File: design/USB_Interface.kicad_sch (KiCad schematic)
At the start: 7 parts, among them J6 USB_C_Receptacle_USB2.0_16P

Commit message: Correccion de algunos DRC
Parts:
- R38: LCSC (none) -> C95177
- R39: LCSC (none) -> C114668
- R40, R41: LCSC (none) -> C107701
- R42, R43: LCSC (none) -> C105580
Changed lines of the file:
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@@
+			)
+		)
+		(property "LCSC" "C107701"
+			(at 138.43 99.06 0)
+			(effects
+				(font
+					(size 1.27 1.27)
+				)
+				(hide yes)
 			)
 		)
@@
 		)
 		(property "MPN" "RC0603FR-075K1L"
+			(at 167.64 107.95 0)
+			(effects
+				(font
+					(size 1.27 1.27)
+				)
+				(hide yes)
+			)
+		)
+		(property "LCSC" "C105580"
 			(at 167.64 107.95 0)
 			(effects
@@
 			)
 		)
+		(property "LCSC" "C95177"
+			(at 111.76 81.28 0)
+			(effects
+				(font
+					(size 1.27 1.27)
+				)
+				(hide yes)
+			)
+		)
 		(pin "1"
 		)
@@
 			)
 		)
+		(property "LCSC" "C107701"
+			(at 138.43 93.98 0)
+			(effects
+				(font
+					(size 1.27 1.27)
+				)
+				(hide yes)
+			)
+		)
 		(pin "1"
 		)
@@
 			)
 		)
+		(property "LCSC" "C105580"
+			(at 157.48 107.95 0)
+			(effects
+				(font
+					(size 1.27 1.27)
+				)
+				(hide yes)
+			)
+		)
 		(pin "1"
 		)
@@
 			(at 121.92 101.6 0)
 			(effects
+				(font
+					(size 1.27 1.27)
+				)
+				(hide yes)
+			)
+		)
+		(property "LCSC" "C114668"
+			(at 121.92 101.6 0)
+			(effects

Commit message: Abaratando costos
Cambios en numeros de jlcpcb, pasados a componentes básicos
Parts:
- J6: now left out of the parts list
- R38: LCSC C95177 -> C21189
- R39: LCSC C114668 -> C22843
- R40, R41: LCSC C107701 -> C23345
- R42, R43: LCSC C105580 -> C23186
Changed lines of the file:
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@@
 			)
 		)
-		(property "LCSC" "C107701"
+		(property "LCSC" "C23345"
 			(at 138.43 99.06 0)
 			(effects
@@
 			)
 		)
-		(property "LCSC" "C105580"
+		(property "LCSC" "C23186"
 			(at 167.64 107.95 0)
 			(effects
@@
 		(unit 1)
 		(exclude_from_sim no)
-		(in_bom yes)
+		(in_bom no)
 		(on_board yes)
 		(dnp no)
@@
 			)
 		)
-		(property "LCSC" "C95177"
+		(property "LCSC" "C21189"
 			(at 111.76 81.28 0)
 			(effects
@@
 			)
 		)
-		(property "LCSC" "C107701"
+		(property "LCSC" "C23345"
 			(at 138.43 93.98 0)
 			(effects
@@
 			)
 		)
-		(property "LCSC" "C105580"
+		(property "LCSC" "C23186"
 			(at 157.48 107.95 0)
 			(effects
@@
 			)
 		)
-		(property "LCSC" "C114668"
+		(property "LCSC" "C22843"
 			(at 121.92 101.6 0)
 			(effects

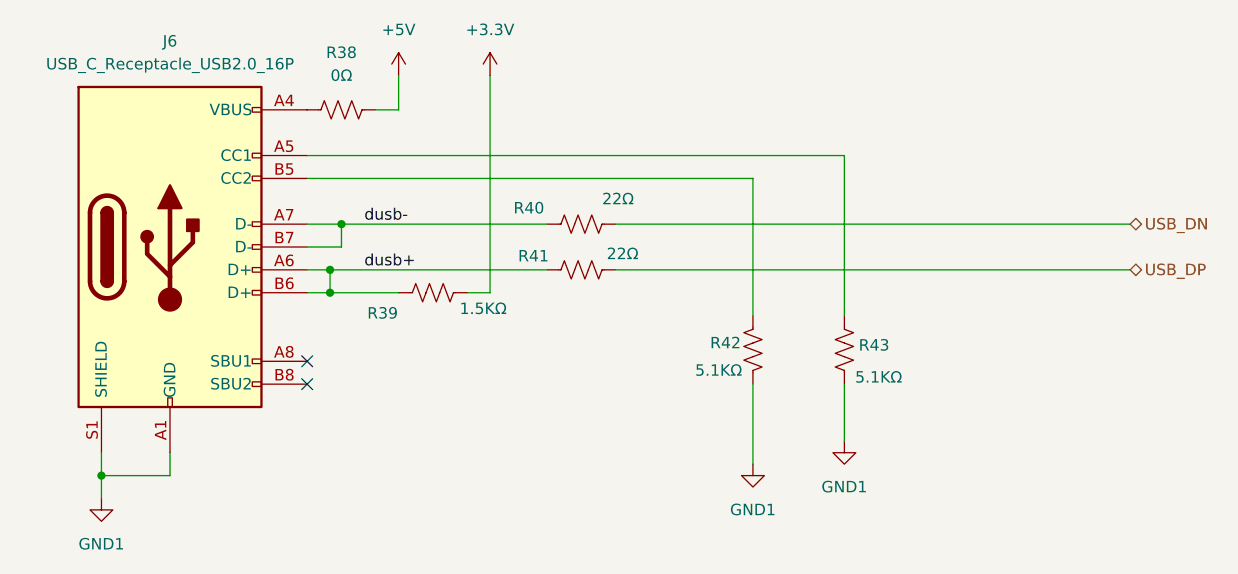
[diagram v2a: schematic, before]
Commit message: Sacado de NRF
Sacado de NRF, re-hecho constraints
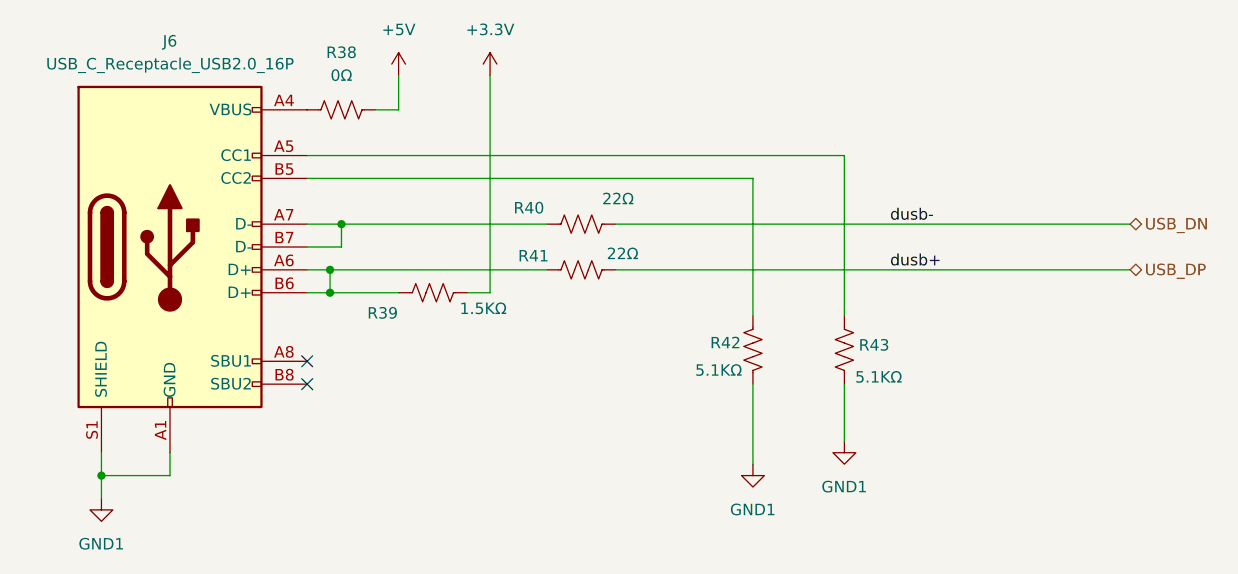
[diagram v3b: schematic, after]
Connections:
- net dusb+: no longer names the net of J6.A6 (D+), J6.B6 (D+), R39.2, R41.2
- net dusb-: no longer names the net of J6.A7 (D-), J6.B7 (D-), R40.2
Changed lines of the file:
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@@
 		)
 	)
-	(label "dusb-"
-		(at 114.3 93.98 0)
+	(label "dusb+"
+		(at 172.72 99.06 0)
 		(fields_autoplaced yes)
 		(effects
@@
 		)
 	)
-	(label "dusb+"
-		(at 114.3 99.06 0)
+	(label "dusb-"
+		(at 172.72 93.98 0)
 		(fields_autoplaced yes)
 		(effects

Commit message: Cambios
Actualizado footprint de USB, cambio de capacitor de feedback por uno básico, pequeños cambios en la ubicación de los footprints.
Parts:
- J6: footprint Connector_USB:USB_C_Receptacle_GCT_USB4105-xx-A_16P_TopMnt_Horizontal -> crf1:USB-SHOUHAN-TYPE-C16PIN; LCSC C3020560 -> C393939; MPN USB4105-GF-A -> (none); Manufacturer Global Connector Technology -> (none); now in the parts list
- R38: MPN RC0603JR-070RL -> (none); Manufacturer YAGEO -> (none)
- R39: MPN RC0603FR-071K5L -> (none); Manufacturer YAGEO -> (none)
- R40, R41: MPN RC0603FR-0722RL -> (none); Manufacturer YAGEO -> (none)
- R42, R43: MPN RC0603FR-075K1L -> (none); Manufacturer YAGEO -> (none)
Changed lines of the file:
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@@
-			)
-		)
-		(property "Manufacturer" "YAGEO"
-			(at 138.43 99.06 0)
-			(effects
-				(font
-					(size 1.27 1.27)
-				)
-				(hide yes)
-			)
-		)
-		(property "MPN" "RC0603FR-0722RL"
-			(at 138.43 99.06 0)
-			(effects
-				(font
-					(size 1.27 1.27)
-				)
-				(hide yes)
 			)
 		)
@@
 			)
 		)
-		(property "Manufacturer" "YAGEO"
-			(at 167.64 107.95 0)
-			(effects
-				(font
-					(size 1.27 1.27)
-				)
-				(hide yes)
-			)
-		)
-		(property "MPN" "RC0603FR-075K1L"
-			(at 167.64 107.95 0)
-			(effects
-				(font
-					(size 1.27 1.27)
-				)
-				(hide yes)
-			)
-		)
 		(property "LCSC" "C23186"
 			(at 167.64 107.95 0)
@@
 		(unit 1)
 		(exclude_from_sim no)
-		(in_bom no)
+		(in_bom yes)
 		(on_board yes)
 		(dnp no)
@@
 			)
 		)
-		(property "Footprint" "Connector_USB:USB_C_Receptacle_GCT_USB4105-xx-A_16P_TopMnt_Horizontal"
+		(property "Footprint" "crf1:USB-SHOUHAN-TYPE-C16PIN"
 			(at 96.52 96.52 0)
 			(effects
@@
 			)
 		)
-		(property "Manufacturer" "Global Connector Technology"
-			(at 92.71 96.52 0)
-			(effects
-				(font
-					(size 1.27 1.27)
-				)
-				(hide yes)
-			)
-		)
-		(property "MPN" "USB4105-GF-A"
-			(at 92.71 96.52 0)
-			(effects
-				(font
-					(size 1.27 1.27)
-				)
-				(hide yes)
-			)
-		)
-		(property "LCSC" "C3020560"
+		(property "LCSC" "C393939"
 			(at 92.71 73.66 0)
 			(effects
@@
 			)
 		)
-		(property "Manufacturer" "YAGEO"
-			(at 111.76 81.28 0)
-			(effects
-				(font
-					(size 1.27 1.27)
-				)
-				(hide yes)
-			)
-		)
-		(property "MPN" "RC0603JR-070RL"
-			(at 111.76 81.28 0)
-			(effects
-				(font
-					(size 1.27 1.27)
-				)
-				(hide yes)
-			)
-		)
 		(property "LCSC" "C21189"
 			(at 111.76 81.28 0)
@@
 			)
 		)
-		(property "Manufacturer" "YAGEO"
-			(at 138.43 93.98 0)
-			(effects
-				(font
-					(size 1.27 1.27)
-				)
-				(hide yes)
-			)
-		)
-		(property "MPN" "RC0603FR-0722RL"
-			(at 138.43 93.98 0)
-			(effects
-				(font
-					(size 1.27 1.27)
-				)
-				(hide yes)
-			)
-		)
 		(property "LCSC" "C23345"
 			(at 138.43 93.98 0)
@@
 			)
 		)
-		(property "Manufacturer" "YAGEO"
-			(at 157.48 107.95 0)
-			(effects
-				(font
-					(size 1.27 1.27)
-				)
-				(hide yes)
-			)
-		)
-		(property "MPN" "RC0603FR-075K1L"
-			(at 157.48 107.95 0)
-			(effects
-				(font
-					(size 1.27 1.27)
-				)
-				(hide yes)
-			)
-		)
 		(property "LCSC" "C23186"
 			(at 157.48 107.95 0)
@@
 			(at 121.92 101.6 0)
 			(effects
-				(font
-					(size 1.27 1.27)
-				)
-				(hide yes)
-			)
-		)
-		(property "Manufacturer" "YAGEO"
-			(at 121.92 101.6 0)
-			(effects
-				(font
-					(size 1.27 1.27)
-				)
-				(hide yes)
-			)
-		)
-		(property "MPN" "RC0603FR-071K5L"
-			(at 121.92 101.6 0)
-			(effects
